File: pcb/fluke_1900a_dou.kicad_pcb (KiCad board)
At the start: 2 copper layers, 69.5 x 53.5 mm, 71 parts, among them J3 DOU CONNECTOR, P3 USB_B, Q1 Si2336DS, Q2 Si2336DS, Q3 Si2336DS, Q4 Si2336DS, U1 TPS71533, U2 MSP430G2452IN20, U3 SFH617A-4, U4 SFH617A-4, U5 SFH617A-4, U6 CH340N, X1 DEBUG

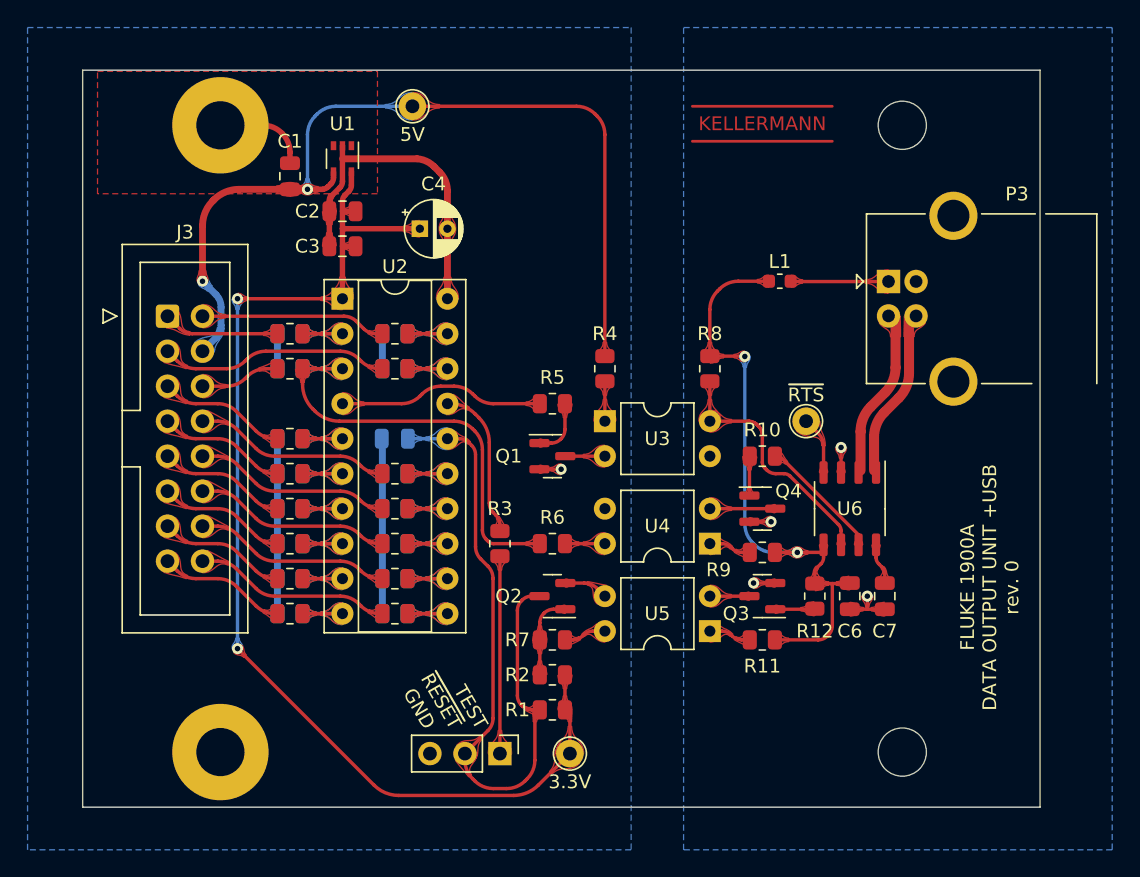
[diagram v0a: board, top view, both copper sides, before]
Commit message: Tx must be connected to RXD on the CH340N
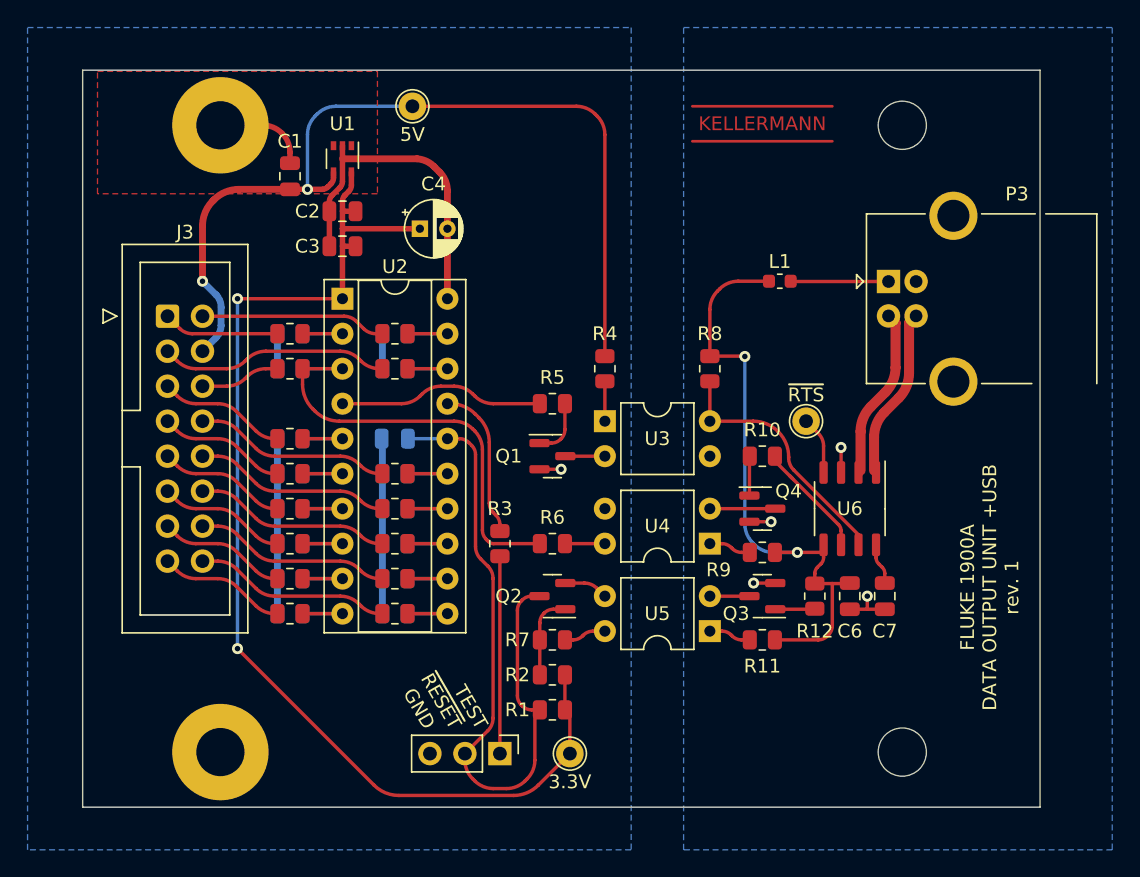
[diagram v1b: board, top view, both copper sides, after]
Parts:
- R11, R4, R9: value 510R 0805 -> 390R 0805
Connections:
- R10 pad 1: /RXD -> /TXD
- R8 pad 1: /TXD -> /RXD
- U3 pad 4: /TXD -> /RXD
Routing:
- net /RXD: track 8.80 -> 18.5 mm
- net /TXD: track 18.2 -> 8.63 mm
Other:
- board text added: "FLUKE 1900A DATA OUTPUT UNIT +USB rev. 1"
- board text removed: "FLUKE 1900A DATA OUTPUT UNIT +USB rev. 0"

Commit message: add fuses F1, F2 to protect device and USB host
In case in anything ever does go wrong, the fuse should protect the
device from any harm. The same makes sense for the USB side of things.
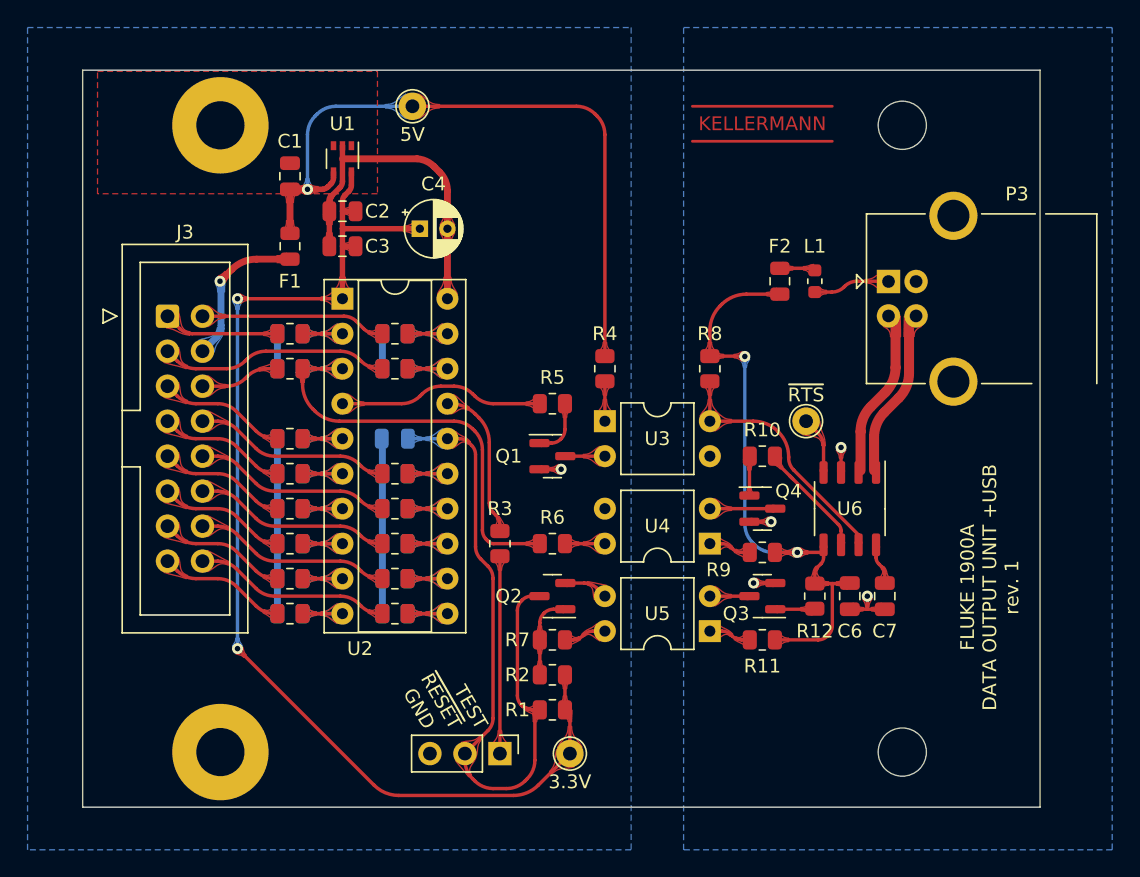
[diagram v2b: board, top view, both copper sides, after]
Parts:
- added F1: 100mA 0805, Fuse:Fuse_0805_2012Metric, F.Cu at (135.6, 86.0)
- added F2: 100mA 0805, Fuse:Fuse_0805_2012Metric, F.Cu at (171.1, 88.6)
- R8: value 10k -> 4k7
- moved L1 2.54 mm to (173.7, 88.6), turned to -90 degrees
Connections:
- J3 pad 4: +5V -> Net-(J3-Pad4)
- L1 pad 1: VBUS -> Net-(L1-Pad1)
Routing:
- net +5V: track 65.5 -> 50.8 mm, vias 2 -> 1
- net Net-(J3-Pad4): track 0.00 -> 11.2 mm, vias 0 -> 1
- net GND: track 63.4 -> 59.6 mm
- net Net-(L1-Pad1): track 0.00 -> 2.60 mm
- net Net-(L1-Pad2): track 7.08 -> 5.56 mm

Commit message: add pull-up R13 to Rx line
While the Rx line is currently not usable, it should be able to operate
at the same bitrate as the Tx line. That requires the ability to select
the pull-up accordingly.
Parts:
- added R13: DNP, Resistor_SMD:R_0805_2012Metric, F.Cu at (135.6, 97.5)
- renumbered R21 to R20, R22 to R21, R23 to R22, R13 to R28, R14 to R29, R15 to R30, R16 to R31, R17 to R32, R18 to R33, R19 to R34, R20 to R35, R41 to R36, R42 to R37, R28 to R38, R29 to R39, R30 to R40, R31 to R41, R34 to R42, R32 to R43, R33 to R44, R35 to R45, R36 to R46, R37 to R47, R38 to R48, R39 to R49, R40 to R50
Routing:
- net +3V3: track 85.4 -> 87.9 mm, vias 2 -> 3
- net /TXD: track 8.63 -> 8.04 mm

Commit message: put a comment regarding mounting
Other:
- board text added: "Matching holes on main PCB: 3.55 mm. Standoff height: 22 mm."
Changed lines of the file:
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@@
     (effects (font (size 1 1) (thickness 0.15)) (justify right))
+  )
+  (gr_text "Matching holes on main PCB: 3.55 mm.\nStandoff height: 22 mm." (at 173.015 66.345) (layer "Cmts.User")
+    (effects (font (size 1 1) (thickness 0.15)) (justify left))
   )
   (dimension (type aligned) (layer "F.Cu")
